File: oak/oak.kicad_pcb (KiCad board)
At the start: 2 copper layers, 77.4 x 128.5 mm, 105 parts, among them J13 Conn_02x05_Odd_Even, J14 Conn_01x03, J15 Conn_01x03, J16 AudioJack2, J17 AudioJack2, J18 AudioJack2, J19 Conn_01x02, J21 AudioJack2, J22 AudioJack2, J23 AudioJack2, J24 USB_C_Receptacle_USB2.0_16P, Q10 MMBT3904, Q11 MMBT3904, Q12 MMBT3904, Q13 MMBT3904, Q14 MMBT3904, Q15 MMBT3904, Q16 MMBT3904, Q17 MMBT3904, Q18 MMBT3904, Q19 MMBT3904, Q20 MMBT3904, SW10 SW_MEC_5E, SW11 SW_MEC_5E, SW12 SW_Push, SW6 LP4OA1PBCT, SW7 LP4OA1PBCT, SW8 LP4OA1PBCT, SW9 LP4OA1PBCT, U13 74AHCT1G125, U18 74AHCT1G125, U19 74AHCT1G125, U20 NCP1117-3.3_SOT223, U21 W25Q32JVSS, U22 RP2040, U23 NCP1117-5.0_SOT223, Y1 ABM8-272-T3

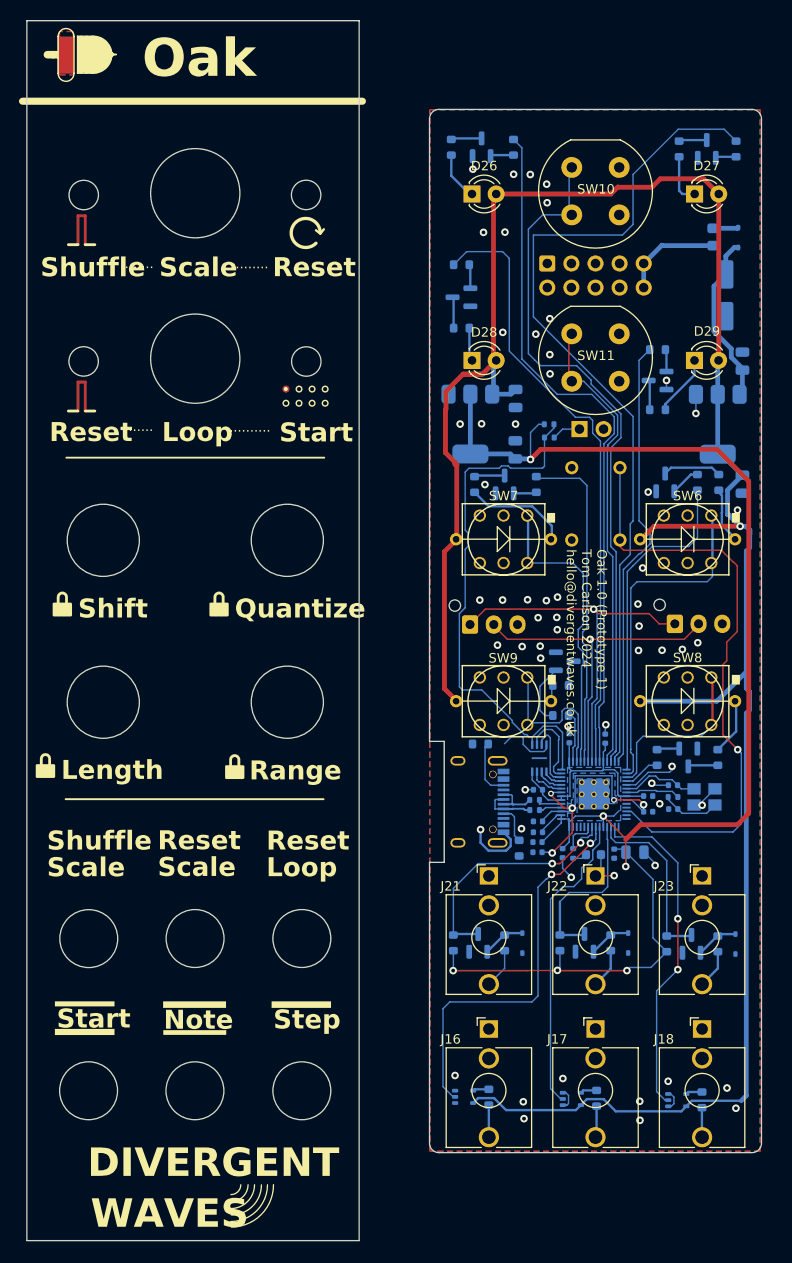
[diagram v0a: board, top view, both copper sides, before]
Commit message: Adding Oak BOM, firmware notes, i2c implementation, design files
Missing assembly instructions, and the firmware for Sycamore needs to be updated as well.
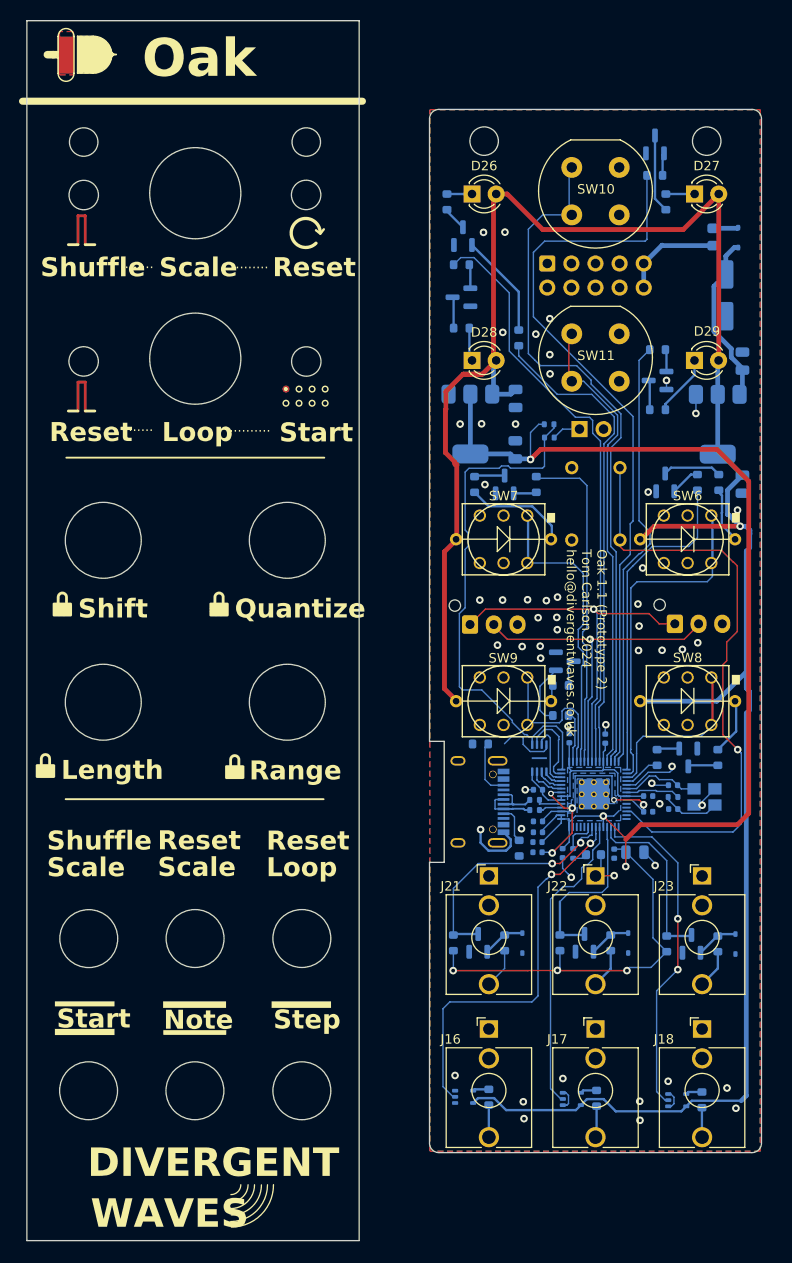
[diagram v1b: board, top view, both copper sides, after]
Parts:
- added H1: MountingHole, MountingHole:MountingHole_3mm, F.Cu at (153.3, 53.1)
- added H2: MountingHole, MountingHole:MountingHole_3mm, F.Cu at (172.0, 53.0)
- added H3: MountingHole, MountingHole:MountingHole_3mm, F.Cu at (195.4, 53.0)
- added H4: MountingHole, MountingHole:MountingHole_3mm, F.Cu at (129.8, 53.1)
- moved R80 20.1 mm to (175.6, 73.7), turned to -90 degrees
- moved Q17 9.56 mm to (169.8, 63.0)
- moved R82 9.01 mm to (190.0, 56.6), turned to 180 degrees
- moved R81 5.77 mm to (168.1, 59.4), turned to -90 degrees
- moved R83 5.75 mm to (191.1, 59.4), turned to -90 degrees
- moved Q18 5.48 mm to (190.0, 53.3)
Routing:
- net /Oak Expander/GPIO7: track 72.8 -> 50.8 mm
- net /Oak Expander/GPIO10: track 90.2 -> 78.1 mm
- net Net-(Q17-B): track 2.46 -> 11.0 mm
- net Net-(Q18-C): track 2.96 -> 8.29 mm
- net /Oak Expander/GPIO6: track 64.8 -> 62.2 mm
- net Net-(D27-K): track 5.35 -> 3.03 mm
- net Net-(D26-K): track 4.89 -> 2.64 mm
- net +5V: track 245.0 -> 246.8 mm
- net Net-(Q17-C): track 3.24 -> 2.54 mm
- net Earth: vias 60 -> 55
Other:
- outline, holes or cut-outs redrawn
- board text added: "Oak 1.1 (Prototype 2) Tom Carlson 2024 hello@divergentwaves.co.uk"
- board text removed: "Oak 1.0 (Prototype 1) Tom Carlson 2024 hello@divergentwaves.co.uk"

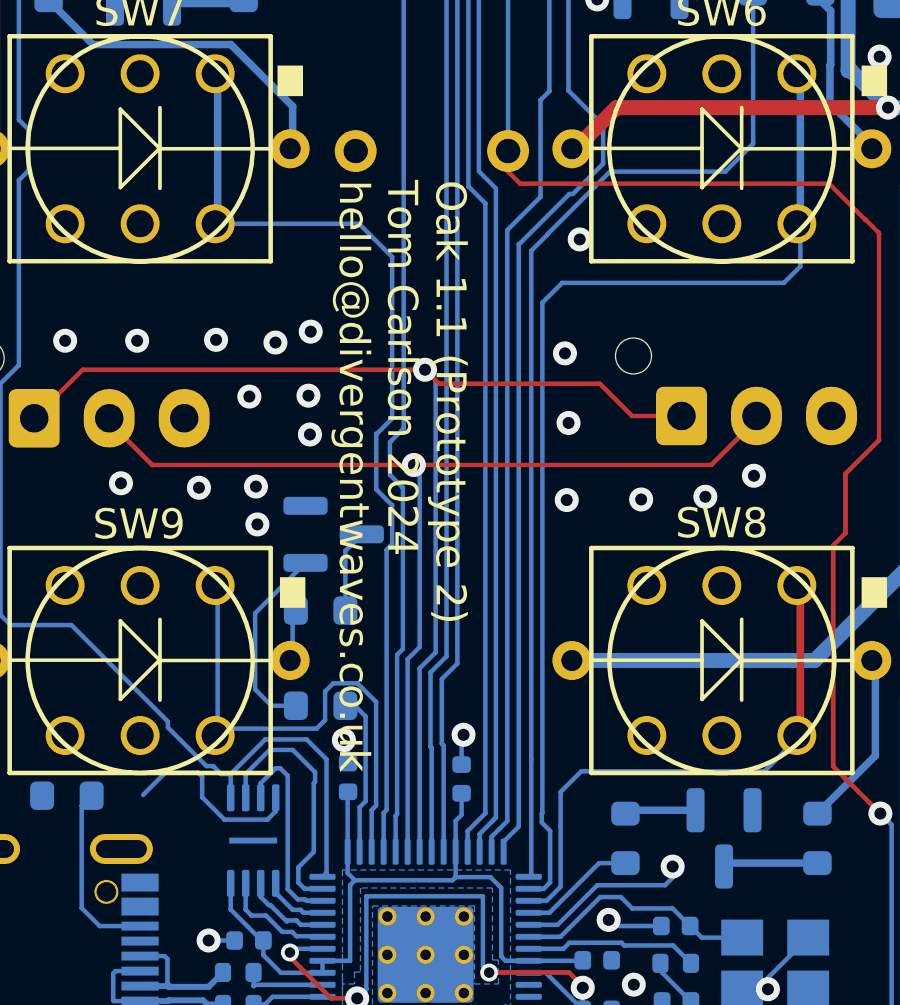
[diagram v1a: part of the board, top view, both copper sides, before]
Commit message: Update Oak's PCBs to production versions; Update Oak's .gitignore to filter local cruft
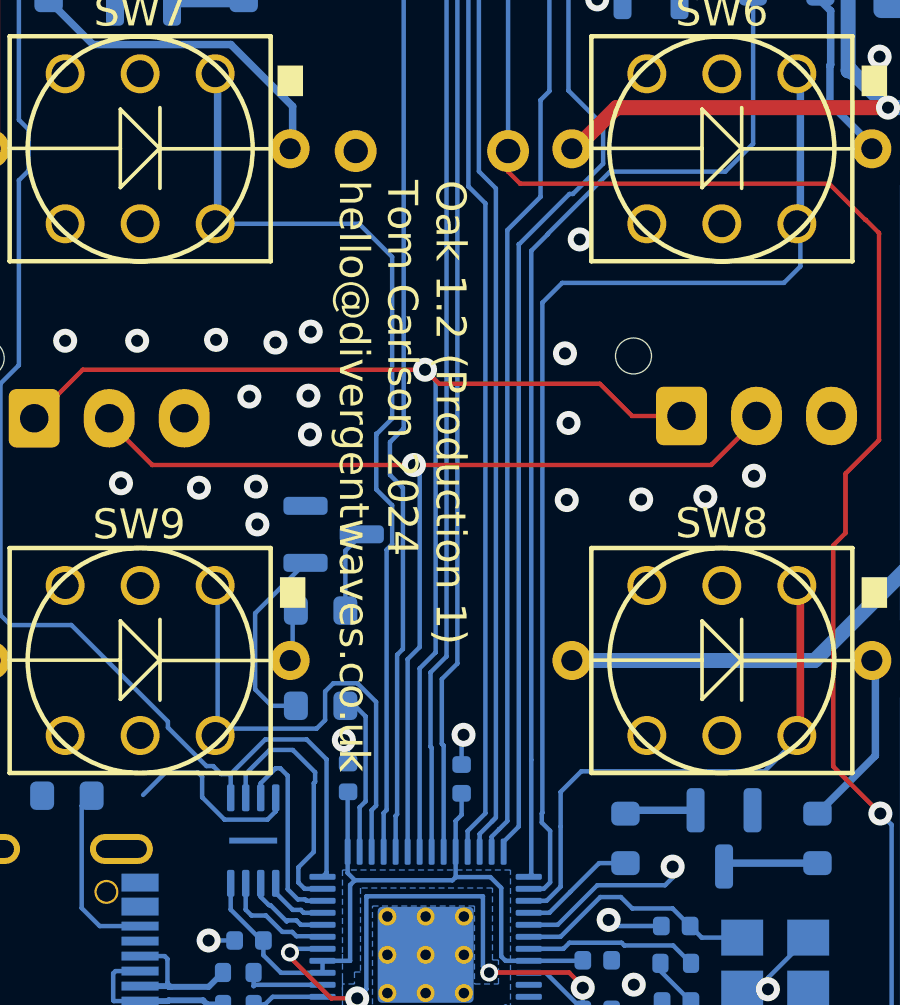
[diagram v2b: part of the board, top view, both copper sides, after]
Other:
- board text added: "Oak 1.2 (Production 1) Tom Carlson 2024 hello@divergentwaves.co.uk"
- board text removed: "Oak 1.1 (Prototype 2) Tom Carlson 2024 hello@divergentwaves.co.uk"
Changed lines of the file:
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@@
 		(layer "Edge.Cuts")
 	)
-	(gr_text "Oak 1.1 (Prototype 2)\nTom Carlson 2024\nhello@divergentwaves.co.uk"
+	(gr_text "Oak 1.2 (Production 1)\nTom Carlson 2024\nhello@divergentwaves.co.uk"
 		(at 151.203 103.611 0)
 		(layer "B.SilkS")
@@
 		)
 	)
-	(gr_text "Oak 1.1 (Prototype 2)\nTom Carlson 2024\nhello@divergentwaves.co.uk"
+	(gr_text "Oak 1.2 (Production 1)\nTom Carlson 2024\nhello@divergentwaves.co.uk"
 		(at 182.773 95.951 270)
 		(layer "F.SilkS")
